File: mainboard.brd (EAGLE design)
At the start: 104.3 x 55.9 mm, 17 parts, among them IC1 7805TV, IC2 7805TV, IC3 7805TV, X1 22-23-2021

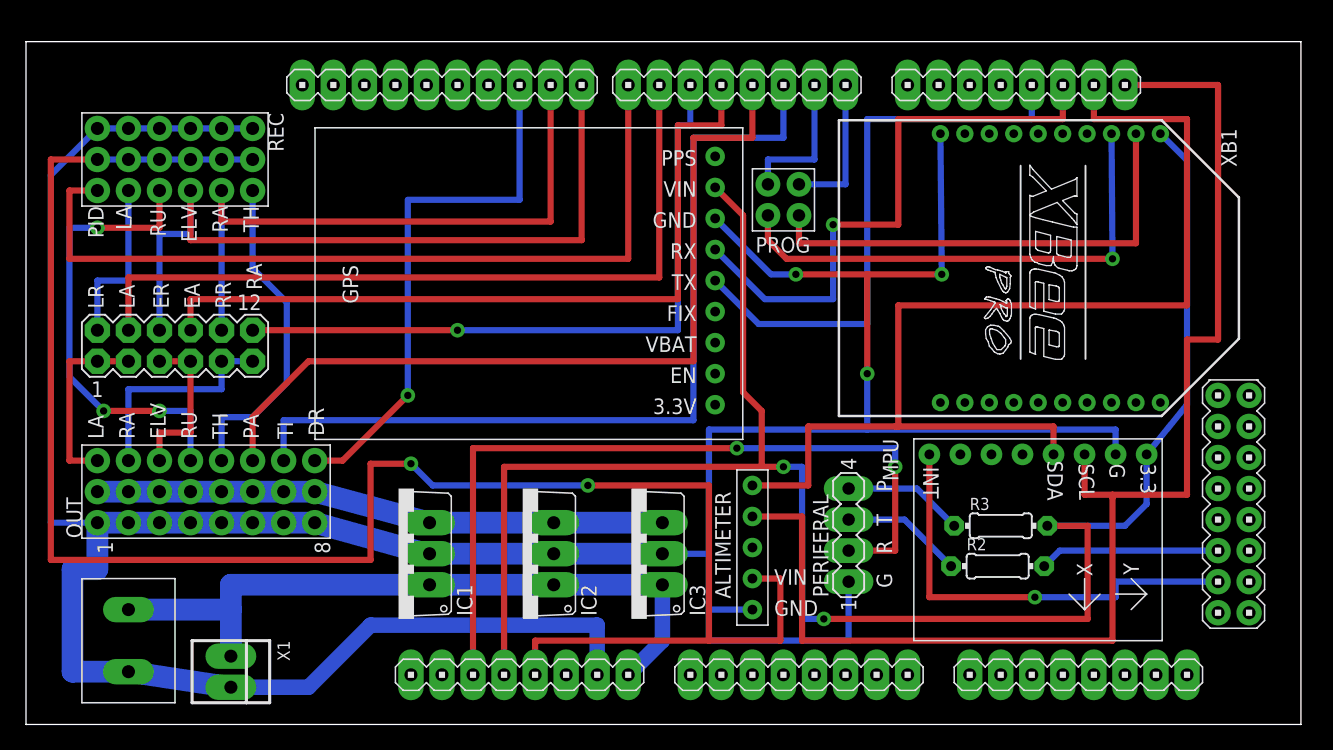
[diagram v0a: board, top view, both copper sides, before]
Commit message: Fix servo connections and remove unnecessary parts
changes from Schindeler's feedback
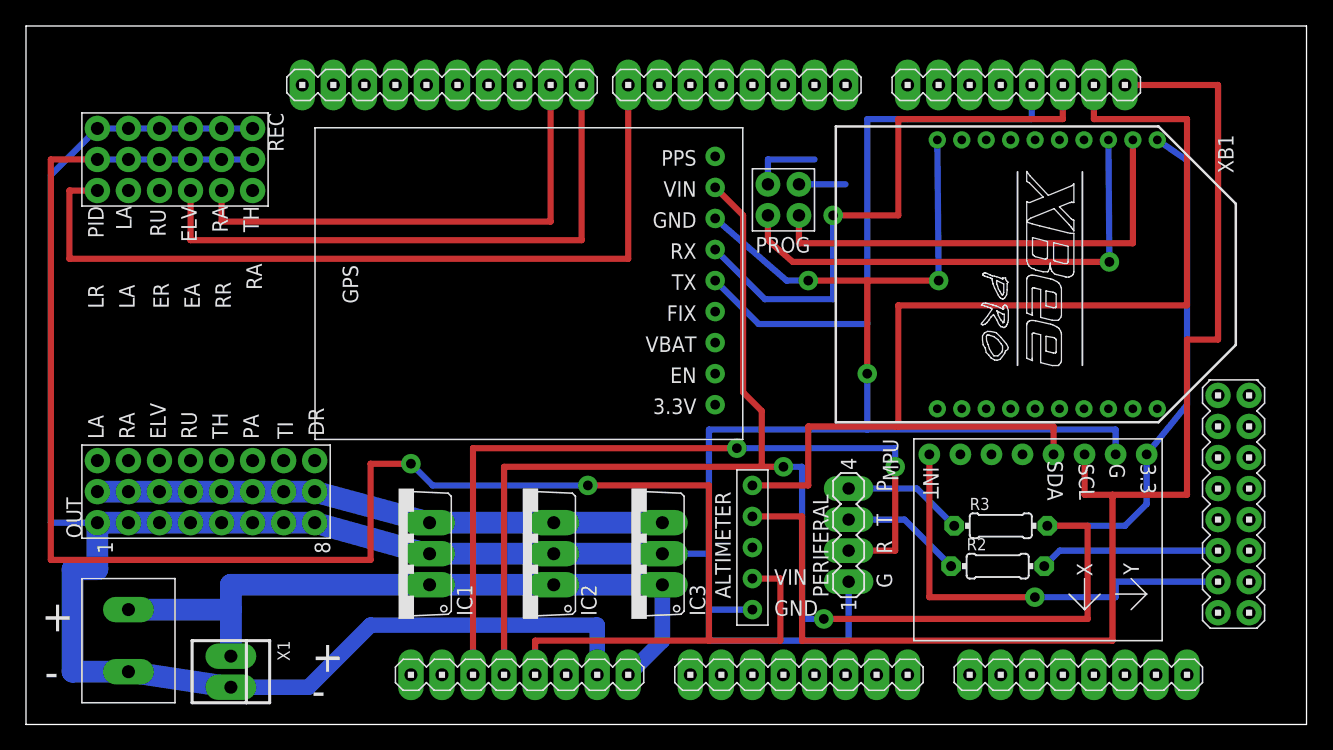
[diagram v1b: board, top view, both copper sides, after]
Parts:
- removed SERVO-CON2: (no value), con-lstb:MA06-2
- moved XB1 0.57 mm to (83.6, 36.8)
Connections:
- removed net CS: U$1.46
- removed net ELEVATOR_A: SERVO-CON2.8, U$1.4
- removed net ELEVATOR_R: REC.3.3, SERVO-CON2.6, U$1.8
- removed net L_AILERON_A: SERVO-CON2.4, U$1.6
- removed net L_AILERON_R: REC.3.5, SERVO-CON2.2
- removed net OUT_ELEVATOR: OUT.3.3, SERVO-CON2.5, SERVO-CON2.7
- removed net OUT_LA: OUT.3.1, SERVO-CON2.1, SERVO-CON2.3
- removed net OUT_RA: OUT.3.2, SERVO-CON2.11, SERVO-CON2.9
- removed net PAN: OUT.3.6, U$1.3
- removed net PS: U$1.48
- removed net R_AILERON_A: SERVO-CON2.12, U$1.5
- removed net R_AILERON_R: REC.3.2, SERVO-CON2.10, U$1.9
- removed net TILT: OUT.3.7, U$1.2
- new net FLAP_MODE: REC.3.5, U$1.11
- new net LEFT_AILERON: OUT.3.1, U$1.6
- new net LEFT_TAIL: OUT.3.3, U$1.3
- new net PITCH_R: REC.3.3, U$1.8
- new net RIGHT_AILERON: OUT.3.2, U$1.5
- new net RIGHT_TAIL: OUT.3.4, U$1.4
- new net ROLL_R: REC.3.2, U$1.9
- new net SPARE: OUT.3.7, U$1.13
- new net YAW_R: REC.3.4, U$1.12
- net RUDDER: now also OUT.3.5, U$1.2; no longer OUT.3.4, REC.3.4
- net RX: now also U$1.RX2; no longer U$1.RX0
- net THROTTLE: now also OUT.3.6; no longer OUT.3.5
- net TX: now also U$1.TX2; no longer U$1.TX0
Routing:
- net TILT: track 71.6 -> 0.00 mm
- net PAN: track 68.9 -> 0.00 mm
- net L_AILERON_A: track 63.5 -> 0.00 mm
- net ELEVATOR_A: track 63.5 -> 0.00 mm
- net ELEVATOR_R: track 62.7 -> 0.00 mm
- net R_AILERON_A: track 55.9 -> 0.00 mm, vias 1 -> 0
- net R_AILERON_R: track 52.1 -> 0.00 mm
- net PITCH_R: track 0.00 -> 48.8 mm
- net DROP: track 44.4 -> 0.00 mm, vias 1 -> 0
- net ROLL_R: track 0.00 -> 40.6 mm
- net RUDDER: track 37.7 -> 0.00 mm, vias 3 -> 0
- net THROTTLE: track 27.0 -> 0.00 mm
- net OUT_RA: track 18.3 -> 0.00 mm
- net OUT_LA: track 15.2 -> 0.00 mm
- net L_AILERON_R: track 14.0 -> 0.00 mm
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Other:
- board size 104.3 x 55.9 mm -> 104.8 x 57.1 mm
- board text added: "+"
- board text added: "-"

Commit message: Update labels on board and servo connections
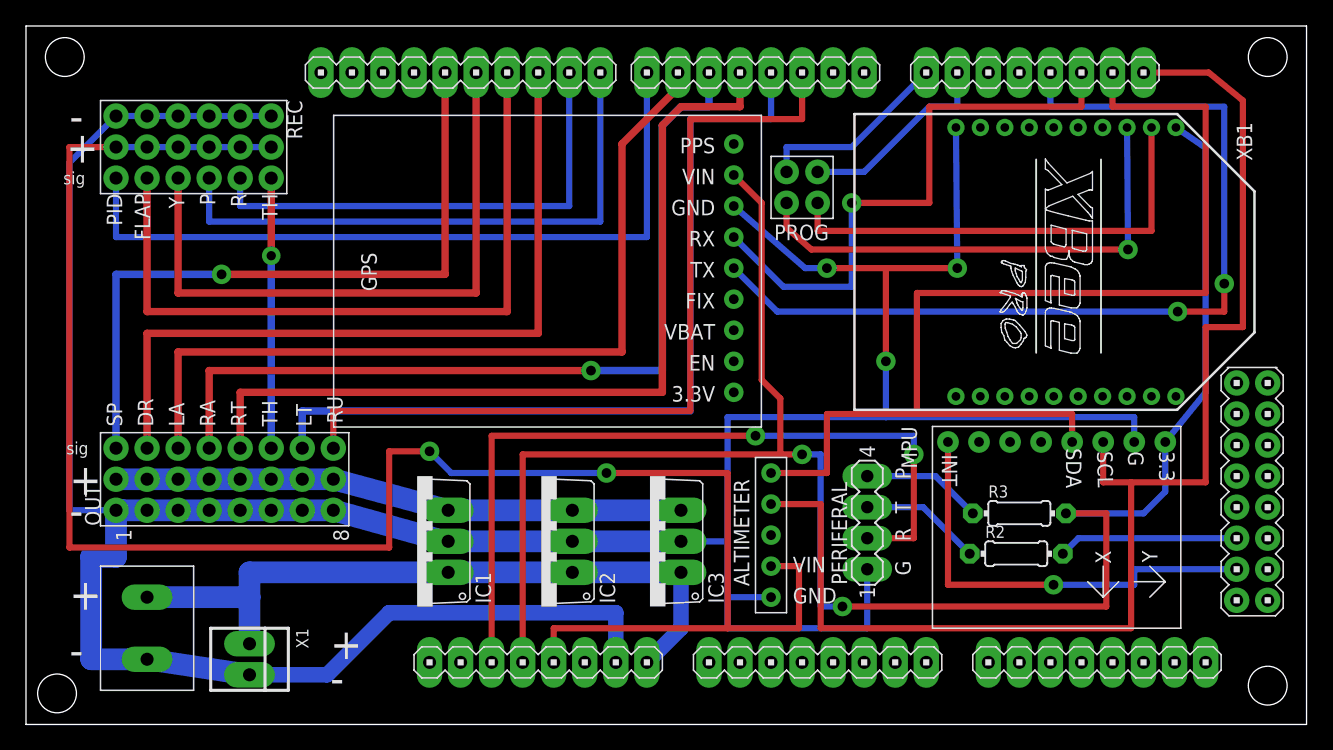
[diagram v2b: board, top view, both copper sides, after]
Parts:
- moved PERIFERAL 1.83 mm to (68.8, 16.5)
- moved IC2 1.83 mm to (42.2, 15.0)
- moved IC3 1.83 mm to (51.1, 15.0)
- moved MPU 1.83 mm to (81.8, 9.14)
- moved R2 1.83 mm to (81.0, 14.0)
- moved U$3 1.83 mm to (9.91, 5.33)
- moved V4 1.83 mm to (61.0, 15.5)
- moved X1 1.83 mm to (18.3, 5.33)
- moved OUT 1.83 mm to (15.0, 17.5)
- moved R3 1.83 mm to (81.3, 17.3)
- moved REC 1.83 mm to (15.0, 49.8)
- moved U$1 1.83 mm to (80.0, 22.9)
- moved U$2 1.83 mm to (63.5, 43.9)
- moved XB1 1.83 mm to (85.1, 37.8)
- moved IC1 1.83 mm to (32.0, 15.0)
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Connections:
- net DROP: now also OUT.3.2; no longer OUT.3.8
- net LEFT_AILERON: now also OUT.3.3; no longer OUT.3.1
- net LEFT_TAIL: now also OUT.3.7; no longer OUT.3.3
- net RIGHT_AILERON: now also OUT.3.4; no longer OUT.3.2
- net RIGHT_TAIL: now also OUT.3.5; no longer OUT.3.4
- net RUDDER: now also OUT.3.8; no longer OUT.3.5
- net RX: now also U$1.RX3; no longer U$1.RX2
- net SPARE: now also OUT.3.1; no longer OUT.3.7
- net TX: now also U$1.TX3; no longer U$1.TX2
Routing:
- net RIGHT_AILERON: track 0.00 -> 70.7 mm, vias 0 -> 1
- net RIGHT_TAIL: track 0.00 -> 70.7 mm
- net LEFT_TAIL: track 0.00 -> 69.1 mm
- net RUDDER: track 0.00 -> 69.1 mm
- net LEFT_AILERON: track 0.00 -> 68.9 mm
- net DROP: track 0.00 -> 62.7 mm
- net FLAP_MODE: track 0.00 -> 59.9 mm
- net SPARE: track 0.00 -> 57.7 mm, vias 0 -> 1
- net YAW_R: track 0.00 -> 51.8 mm
- net TX1: track 46.9 -> 75.4 mm, vias 0 -> 2
- net THROTTLE: track 0.00 -> 22.1 mm, vias 0 -> 1
- net RX: track 3.81 -> 16.4 mm
- net TX: track 5.84 -> 16.0 mm
- net PID_MODE: track 67.8 -> 61.7 mm
- net PITCH_R: track 48.8 -> 47.8 mm
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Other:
- board text added: "FLAP"
- board text added: "LT"
- board text added: "RT"
- board text added: "SP"
- board text added: "Y"
- board text added: "sig"
- board text removed: "EA"
- board text removed: "ELV"
- board text removed: "ER"
- board text removed: "LR"
- board text removed: "PA"
- board text removed: "RR"
- board text removed: "TI"

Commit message: final updates
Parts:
- moved X1 5.24 mm to (23.4, 6.60)
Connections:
- removed net N$1: U$1.GND_1
- net GND: now also U$1.GND_1
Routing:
- net GND: track 281.2 -> 285.1 mm
- net 12V: track 58.1 -> 56.8 mm
